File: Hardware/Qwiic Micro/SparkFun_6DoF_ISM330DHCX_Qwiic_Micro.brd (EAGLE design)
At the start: 19.1 x 7.6 mm, 37 parts, among them J1 Qwiic Right Angle, U1 ISM330DHCX

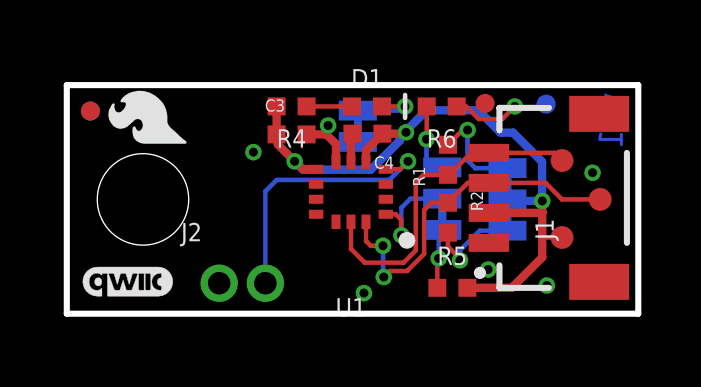
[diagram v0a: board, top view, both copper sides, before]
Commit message: Moves test points to their designated areas, increases the size of most of the silk
* Moves to v10
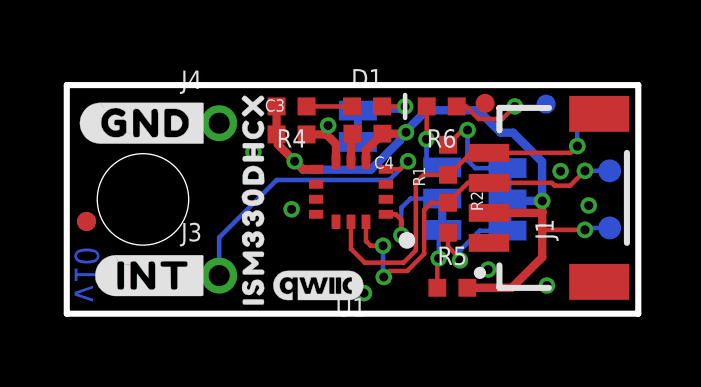
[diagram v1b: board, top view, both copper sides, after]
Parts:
- removed J2: (no value), SparkFun-Connectors:1X02_1.5MM_NO_SILK
- removed U$25: (no value), bot:#I2C#11
- added J3, J4: (no value), SparkFun-Connectors:1X01_1MM_NO_SILK
- added TP4: TEST-POINT3, SparkFun-Connectors:PAD.03X.03
- added U$10: (no value), top:#GND#2
- added U$11: (no value), top:#INT#3
- added U$12: (no value), top:#I2C#4
- U$1: device ISMTopMini:#1#2121 -> top:#0#4
- U$2: device ISMTopMini:#0#2121 -> top:#1#4
- U$4: device ISMTopMini:#INT1#112 -> top:#GND#0
- U$5: device ISMTopMini:#GND#5 -> top:#INT#1
- moved U$29 15.1 mm to (17.7, 6.10), flipped to the bottom, turned to 0 degrees
- moved U$7 8.50 mm to (9.27, 2.03)
- moved U$4 6.47 mm to (2.67, 6.35), flipped to the top
- moved LOGO1 6.35 mm to (8.38, 0.94)
- moved U$5 5.66 mm to (2.92, 1.27), flipped to the top
- moved U$9 5.08 mm to (5.87, 3.35)
- moved U$2 4.85 mm to (12.4, 1.40), turned to 90 degrees
- moved U$1 4.72 mm to (12.6, 6.35)
- moved U$8 4.58 mm to (6.22, 1.57)
- moved FD2 3.69 mm to (0.66, 3.07)
- moved FID2 3.69 mm to (0.66, 3.07)
- moved TP1 2.23 mm to (18.1, 6.67), flipped to the bottom, turned to 270 degrees
- moved TP3 1.62 mm to (18.1, 2.86), flipped to the bottom
- moved U$6 1.40 mm to (6.22, 3.84), flipped to the top
- moved TP2 1.00 mm to (18.1, 4.76), flipped to the bottom
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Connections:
- net GND: now also J4.1, TP4.1; no longer J2.1
- net INT1: now also J3.1; no longer J2.2
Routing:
- net SCL: track 11.1 -> 13.7 mm, vias 0 -> 1
- net 3.3V: track 24.7 -> 26.3 mm, vias 3 -> 4
- net SDA: track 11.9 -> 12.3 mm, vias 2 -> 3
- net GND: vias 7 -> 9
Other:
- board text added: "v10"
- board text removed: "v01"

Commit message: Adds all the measures anyone could want
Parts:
- moved FRAME1 11.7 mm to (-21.6, -22.9)
- moved J1 0.11 mm to (14.0, 3.81)
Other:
- board text added: "Units in Inches"
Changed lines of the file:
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@@
 <layer number="45" name="Holes" color="7" fill="1" visible="yes" active="yes"/>
 <layer number="46" name="Milling" color="3" fill="1" visible="no" active="yes"/>
-<layer number="47" name="Measures" color="7" fill="1" visible="no" active="yes"/>
+<layer number="47" name="Measures" color="7" fill="1" visible="yes" active="yes"/>
 <layer number="48" name="Document" color="7" fill="1" visible="no" active="yes"/>
 <layer number="49" name="Reference" color="13" fill="1" visible="yes" active="yes"/>
@@
 <wire x1="19.05" y1="0" x2="19.05" y2="7.62" width="0.2032" layer="20"/>
 <text x="0.263525" y="0.371475" size="0.8128" layer="16" font="vector" ratio="22" rot="SMR90">v10</text>
-<dimension x1="14.0716" y1="3.8608" x2="13.97" y2="0" x3="22.86" y3="1.9304" textsize="1.778" textratio="15" layer="47" dtype="vertical" unit="inch"/>
 <rectangle x1="9.1948" y1="4.953" x2="9.2456" y2="5.1816" layer="41"/>
-<dimension x1="19.05" y1="8.89" x2="0" y2="8.89" x3="9.525" y3="15.24" textsize="1.778" layer="47" dtype="horizontal" unit="inch"/>
-<dimension x1="2.54" y1="3.81" x2="0" y2="3.81" x3="1.27" y3="11.43" textsize="1.778" layer="47" dtype="horizontal" unit="inch"/>
+<dimension x1="2.54" y1="3.81" x2="0" y2="3.81" x3="1.27" y3="12.7" textsize="1.778" layer="47" dtype="horizontal" unit="inch"/>
 <wire x1="10.541" y1="3.305175" x2="8.636" y2="3.305175" width="0.254" layer="22"/>
 <wire x1="9.144" y1="2.797175" x2="9.144" y2="3.940175" width="0.254" layer="22" curve="180"/>
@@
 <wire x1="8.128" y1="2.921" x2="7.239" y2="3.81" width="0.254" layer="22"/>
 <wire x1="7.366" y1="2.921" x2="8.255" y2="3.81" width="0.254" layer="22"/>
-<dimension x1="0" y1="7.62" x2="0" y2="0" x3="-5.08" y3="3.81" textsize="1.778" layer="47" unit="inch"/>
+<dimension x1="19.05" y1="7.62" x2="0" y2="7.62" x3="9.525" y3="16.51" textsize="1.778" textratio="15" layer="47" unit="inch"/>
+<dimension x1="19.05" y1="0" x2="19.05" y2="7.62" x3="27.94" y3="3.81" textsize="1.778" textratio="15" layer="47" unit="inch"/>
+<dimension x1="2.54" y1="3.81" x2="2.54" y2="0" x3="-10.16" y3="1.905" textsize="1.778" textratio="15" layer="47" unit="inch"/>
+<dimension x1="5.08" y1="1.27" x2="5.08" y2="0" x3="-13.97" y3="0.635" textsize="1.778" textratio="15" layer="47" unit="inch"/>
+<dimension x1="5.08" y1="1.27" x2="0" y2="1.27" x3="2.54" y3="-3.81" textsize="1.778" textratio="15" layer="47" unit="inch"/>
+<dimension x1="5.08" y1="6.35" x2="5.08" y2="1.27" x3="-6.35" y3="3.81" textsize="1.778" textratio="15" layer="47" unit="inch"/>
+<dimension x1="5.08" y1="6.35" x2="19.05" y2="6.35" x3="12.065" y3="10.16" textsize="1.778" textratio="15" layer="47" unit="inch"/>
+<dimension x1="13.97" y1="3.81" x2="13.97" y2="7.62" x3="22.86" y3="5.715" textsize="1.778" textratio="15" layer="47" unit="inch"/>
+<text x="-1.27" y="-10.16" size="1.778" layer="47" font="vector">Units in Inches</text>
 </plain>
 <attributes>
@@
 </autorouter>
 <elements>
-<element name="FRAME1" library="SparkFun-Aesthetics" package="CREATIVE_COMMONS" value="FRAME-LETTER" x="-19.05" y="-11.43" smashed="yes">
-<attribute name="DESIGNER" value="Elias Santistevan" x="12.7" y="-11.43" size="1.778" layer="51" font="vector"/>
-<attribute name="REV" value="" x="-19.05" y="-11.43" size="1.778" layer="27" display="off"/>
+<element name="FRAME1" library="SparkFun-Aesthetics" package="CREATIVE_COMMONS" value="FRAME-LETTER" x="-21.59" y="-22.86" smashed="yes">
+<attribute name="DESIGNER" value="Elias Santistevan" x="10.16" y="-22.86" size="1.778" layer="51" font="vector"/>
+<attribute name="REV" value="" x="-21.59" y="-22.86" size="1.778" layer="27" display="off"/>
 </element>
 <element name="C3" library="SparkFun-Capacitors" package="0402-TIGHT" value="0.1uF" x="7.493" y="5.97535" smashed="yes">
@@
 <attribute name="VALUE" x="12.4968" y="7.6708" size="0.6096" layer="27" font="vector" ratio="20" rot="R180" align="top-center"/>
 </element>
-<element name="J1" library="SparkFun-Connectors" package="JST04_1MM_RA" value="Qwiic Right Angle" x="14.0716" y="3.8608" smashed="yes" rot="R90">
-<attribute name="NAME" x="16.2306" y="2.4638" size="0.6096" layer="25" font="vector" ratio="20" rot="R90"/>
-<attribute name="PROD_ID" value="CONN-13694" x="14.0716" y="3.8608" size="1.778" layer="27" rot="R90" display="off"/>
-<attribute name="VALUE" x="17.3736" y="2.2098" size="0.6096" layer="27" font="vector" ratio="20" rot="R90"/>
+<element name="J1" library="SparkFun-Connectors" package="JST04_1MM_RA" value="Qwiic Right Angle" x="13.97" y="3.81" smashed="yes" rot="R90">
+<attribute name="NAME" x="16.129" y="2.413" size="0.6096" layer="25" font="vector" ratio="20" rot="R90"/>
+<attribute name="PROD_ID" value="CONN-13694" x="13.97" y="3.81" size="1.778" layer="27" rot="R90" display="off"/>
+<attribute name="VALUE" x="17.272" y="2.159" size="0.6096" layer="27" font="vector" ratio="20" rot="R90"/>
 </element>
 <element name="LOGO1" library="SparkFun-Aesthetics" package="QWIIC_3MM" value="QWIIC_LOGO_3MM" x="8.382" y="0.9398" smashed="yes"/>
@@
 <wire x1="9.4742" y1="3.064" x2="9.4742" y2="2.159" width="0.1524" layer="1"/>
 <wire x1="9.9314" y1="1.7018" x2="9.4742" y2="2.159" width="0.1524" layer="1"/>
-<wire x1="14.0716" y1="5.3608" x2="13.47903125" y2="5.3608" width="0.1524" layer="1"/>
-<wire x1="12.70635" y1="4.6308" x2="12.74903125" y2="4.6308" width="0.1524" layer="1"/>
-<wire x1="13.47903125" y1="5.3608" x2="12.74903125" y2="4.6308" width="0.1524" layer="1"/>
+<wire x1="12.74903125" y1="4.6308" x2="12.70635" y2="4.6308" width="0.1524" layer="1"/>
 <wire x1="12.70635" y1="4.6308" x2="11.8952" y2="4.6308" width="0.1524" layer="1"/>
 <wire x1="11.2268" y1="1.7018" x2="9.9314" y2="1.7018" width="0.1524" layer="1"/>
@@
 <wire x1="11.6332" y1="2.1082" x2="11.2268" y2="1.7018" width="0.1524" layer="1"/>
 <contactref element="TP1" pad="1"/>
-<wire x1="14.0716" y1="5.3608" x2="16.7908" y2="5.3608" width="0.1524" layer="1"/>
 <wire x1="16.7908" y1="5.3608" x2="17.018" y2="5.588" width="0.1524" layer="1"/>
 <via x="17.018" y="5.588" extent="1-16" drill="0.3048"/>
@@
 <wire x1="17.2085" y1="6.6675" x2="18.0975" y2="6.6675" width="0.1524" layer="16"/>
 <wire x1="17.018" y1="6.477" x2="17.2085" y2="6.6675" width="0.1524" layer="16"/>
+<wire x1="13.97" y1="5.31" x2="13.42823125" y2="5.31" width="0.1524" layer="1"/>
+<wire x1="13.42823125" y1="5.31" x2="12.74903125" y2="4.6308" width="0.1524" layer="1"/>
+<wire x1="13.97" y1="5.31" x2="14.0208" y2="5.3608" width="0.1524" layer="1"/>
+<wire x1="14.0208" y1="5.3608" x2="16.7908" y2="5.3608" width="0.1524" layer="1"/>
 </signal>
 <signal name="SDA">
@@
 <wire x1="10.541" y1="2.26455" x2="10.13065" y2="2.26455" width="0.1524" layer="1"/>
 <wire x1="10.13065" y1="2.26455" x2="9.9742" y2="2.421" width="0.1524" layer="1"/>
-<wire x1="14.0716" y1="4.3608" x2="13.36675" y2="4.3608" width="0.1524" layer="1"/>
-<wire x1="13.36675" y1="4.3608" x2="12.70635" y2="3.7004" width="0.1524" layer="1"/>
 <wire x1="12.70635" y1="3.7004" x2="12.1586" y2="3.7004" width="0.1524" layer="1"/>
 <via x="10.5664" y="1.2216" extent="1-16" drill="0.3"/>
@@
 <wire x1="17.272" y1="4.7625" x2="18.0975" y2="4.7625" width="0.1524" layer="16"/>
 <via x="17.272" y="4.7625" extent="1-16" drill="0.3048"/>
-<wire x1="16.16909375" y1="4.3608" x2="16.26029375" y2="4.2696" width="0.1524" layer="1"/>
+<wire x1="16.7791" y1="4.2696" x2="17.272" y2="4.7625" width="0.1524" layer="1"/>
+<wire x1="13.97" y1="4.31" x2="16.21989375" y2="4.31" width="0.1524" layer="1"/>
+<wire x1="16.21989375" y1="4.31" x2="16.26029375" y2="4.2696" width="0.1524" layer="1"/>
 <wire x1="16.26029375" y1="4.2696" x2="16.7791" y2="4.2696" width="0.1524" layer="1"/>
-<wire x1="16.7791" y1="4.2696" x2="17.272" y2="4.7625" width="0.1524" layer="1"/>
-<wire x1="14.0716" y1="4.3608" x2="16.16909375" y2="4.3608" width="0.1524" layer="1"/>
+<wire x1="13.97" y1="4.31" x2="13.31595" y2="4.31" width="0.1524" layer="1"/>
+<wire x1="13.31595" y1="4.31" x2="12.70635" y2="3.7004" width="0.1524" layer="1"/>
 </signal>
 <signal name="SA0">
@@
 <wire x1="7.8799" y1="4.814" x2="8.3117" y2="4.814" width="0.2794" layer="1"/>
 <wire x1="7.8799" y1="4.814" x2="7.6139" y2="5.08" width="0.2794" layer="1"/>
-<wire x1="15.8322" y1="3.3608" x2="15.8496" y2="3.3782" width="0.2794" layer="1"/>
-<wire x1="14.0716" y1="3.3608" x2="15.8322" y2="3.3608" width="0.2794" layer="1"/>
 <wire x1="14.464040625" y1="6.033759375" x2="13.716" y2="6.7818" width="0.2794" layer="16"/>
 <wire x1="13.716" y1="6.7818" x2="11.9936" y2="6.7818" width="0.2794" layer="16"/>
@@
 <via x="17.272" y="2.794" extent="1-16" drill="0.3048"/>
 <wire x1="17.272" y1="2.794" x2="15.8496" y2="2.794" width="0.1524" layer="1"/>
+<wire x1="13.97" y1="3.31" x2="14.0382" y2="3.3782" width="0.2794" layer="1"/>
+<wire x1="14.0382" y1="3.3782" x2="15.8496" y2="3.3782" width="0.2794" layer="1"/>
 </signal>
 <signal name="N$5">
@@
 <contactref element="I2C_PU" pad="3"/>
 <contactref element="R2" pad="2"/>
-<via x="13.107228125" y="1.778828125" extent="1-16" drill="0.3"/>
+<via x="13.107228125" y="1.651828125" extent="1-16" drill="0.3"/>
 <wire x1="12.70635" y1="2.7004" x2="12.70635" y2="2.23735625" width="0.1524" layer="1"/>
 <wire x1="13.7668" y1="2.7686" x2="13.107228125" y2="2.109028125" width="0.1524" layer="16"/>
-<wire x1="13.107228125" y1="1.778828125" x2="13.107228125" y2="2.109028125" width="0.1524" layer="16"/>
+<wire x1="13.107228125" y1="1.651828125" x2="13.107228125" y2="2.109028125" width="0.1524" layer="16"/>
 <wire x1="13.7668" y1="2.7686" x2="14.68755" y2="2.7686" width="0.1524" layer="16"/>
-<wire x1="13.107228125" y1="1.836478125" x2="13.107228125" y2="1.778828125" width="0.1524" layer="1"/>
+<wire x1="13.107228125" y1="1.836478125" x2="13.107228125" y2="1.651828125" width="0.1524" layer="1"/>
 <wire x1="12.70635" y1="2.23735625" x2="13.107228125" y2="1.836478125" width="0.1524" layer="1"/>
 </signal>

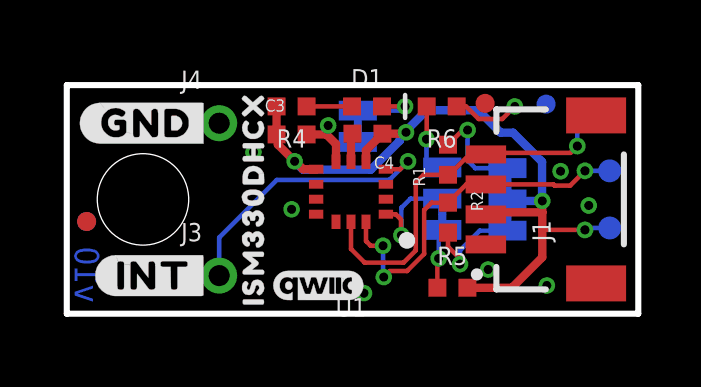
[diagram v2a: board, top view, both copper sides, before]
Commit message: adds 10k pullup on CS
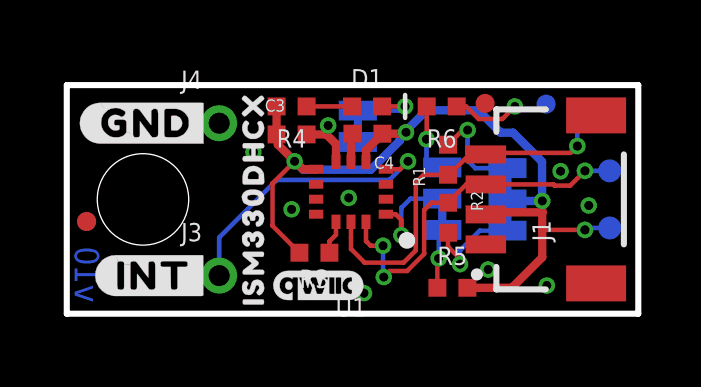
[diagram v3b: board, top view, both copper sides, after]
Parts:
- added R3: 10k, SparkFun-Resistors:0402-TIGHT
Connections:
- new net N$4: R3.1, U1.P12
- net 3.3V: now also R3.2
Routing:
- net 3.3V: track 26.5 -> 30.2 mm
- net N$4: track 0.00 -> 1.12 mm
- net GND: vias 9 -> 10
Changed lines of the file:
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@@
 <layer number="37" name="tTest" color="7" fill="1" visible="no" active="yes"/>
 <layer number="38" name="bTest" color="7" fill="1" visible="no" active="yes"/>
-<layer number="39" name="tKeepout" color="4" fill="11" visible="yes" active="yes"/>
+<layer number="39" name="tKeepout" color="4" fill="11" visible="no" active="yes"/>
 <layer number="40" name="bKeepout" color="1" fill="11" visible="no" active="yes"/>
 <layer number="41" name="tRestrict" color="4" fill="10" visible="no" active="yes"/>
@@
 <layer number="45" name="Holes" color="7" fill="1" visible="yes" active="yes"/>
 <layer number="46" name="Milling" color="3" fill="1" visible="no" active="yes"/>
-<layer number="47" name="Measures" color="7" fill="1" visible="yes" active="yes"/>
+<layer number="47" name="Measures" color="7" fill="1" visible="no" active="yes"/>
 <layer number="48" name="Document" color="7" fill="1" visible="no" active="yes"/>
 <layer number="49" name="Reference" color="13" fill="1" visible="yes" active="yes"/>
@@
 <element name="U$2" library="top" package="#1#4" value="" x="12.446" y="1.397" smashed="yes" rot="MR90"/>
 <element name="U$12" library="top" package="#I2C#4" value="" x="16.383" y="3.81" smashed="yes" rot="MR90"/>
+<element name="R3" library="SparkFun-Resistors" package="0402-TIGHT" value="10k" x="8.255" y="2.032" smashed="yes" rot="R180">
+<attribute name="NAME" x="8.255" y="1.47" size="0.6096" layer="25" font="vector" ratio="20" rot="R180" align="bottom-center"/>
+<attribute name="PROD_ID" value="RES-14241" x="8.255" y="2.032" size="1.778" layer="27" font="vector" ratio="15" rot="R180" display="off"/>
+<attribute name="VALUE" x="8.255" y="2.594" size="0.6096" layer="27" font="vector" ratio="20" rot="R180" align="top-center"/>
+</element>
 </elements>
 <signals>
@@
 <via x="7.493" y="3.4798" extent="1-16" drill="0.3"/>
 <via x="16.4592" y="4.7498" extent="1-16" drill="0.3"/>
+<via x="9.398" y="3.8608" extent="1-16" drill="0.3"/>
 </signal>
 <signal name="SCL">
@@
 <contactref element="U1" pad="P13"/>
 <contactref element="J1" pad="4"/>
-<wire x1="9.4742" y1="3.064" x2="9.4742" y2="2.159" width="0.1524" layer="1"/>
+<wire x1="9.4742" y1="3.064" x2="9.4742" y2="2.54" width="0.1524" layer="1"/>
+<wire x1="9.4742" y1="2.54" x2="9.4742" y2="2.159" width="0.1524" layer="1"/>
 <wire x1="9.9314" y1="1.7018" x2="9.4742" y2="2.159" width="0.1524" layer="1"/>
 <wire x1="12.74903125" y1="4.6308" x2="12.70635" y2="4.6308" width="0.1524" layer="1"/>
@@
 <wire x1="13.97" y1="3.31" x2="14.0382" y2="3.3782" width="0.2794" layer="1"/>
 <wire x1="14.0382" y1="3.3782" x2="15.8496" y2="3.3782" width="0.2794" layer="1"/>
+<contactref element="R3" pad="2"/>
+<wire x1="7.755" y1="2.032" x2="6.858" y2="2.929" width="0.1524" layer="1"/>
+<wire x1="6.858" y1="4.3434" x2="7.5946" y2="5.08" width="0.1524" layer="1"/>
+<wire x1="6.858" y1="2.929" x2="6.858" y2="4.3434" width="0.1524" layer="1"/>
 </signal>
 <signal name="N$5">
@@
 <wire x1="12.13485" y1="4.8768" x2="11.9888" y2="5.02285" width="0.1524" layer="16"/>
 </signal>
+<signal name="N$4">
+<contactref element="U1" pad="P12"/>
+<contactref element="R3" pad="1"/>
+<wire x1="8.9742" y1="3.064" x2="8.9742" y2="2.6322" width="0.1524" layer="1"/>
+<wire x1="8.9742" y1="2.6322" x2="8.755" y2="2.413" width="0.1524" layer="1"/>
+<wire x1="8.755" y1="2.413" x2="8.755" y2="2.032" width="0.1524" layer="1"/>
+</signal>
 </signals>
